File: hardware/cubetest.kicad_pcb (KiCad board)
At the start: 2 copper layers, 50.8 x 50.8 mm, 22 parts, among them J1 In, J10 GS2, J11 GS2, J2 Out, J3 pwr1, J4 pwr2, J5 USB_OTG, J6 GS3, J7 GS3, J8 GS3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

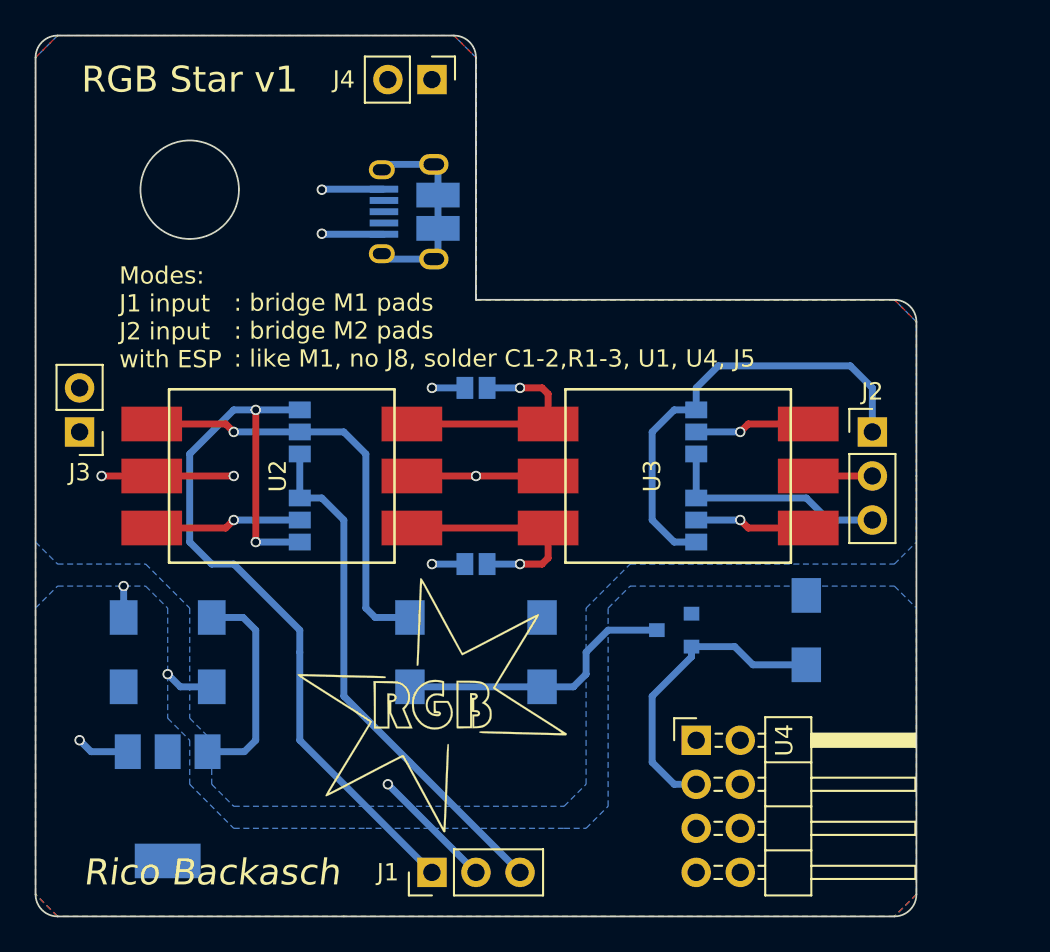
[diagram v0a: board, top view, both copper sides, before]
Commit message: remove solder bridges
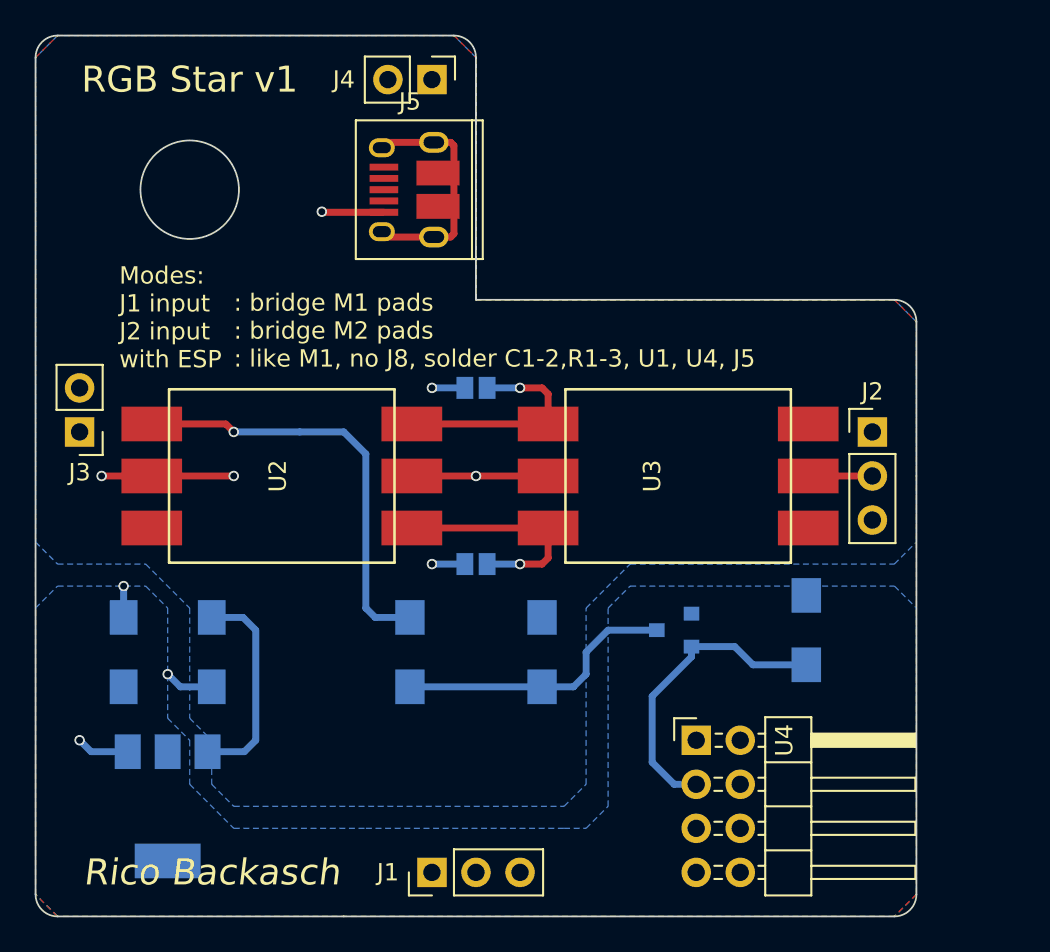
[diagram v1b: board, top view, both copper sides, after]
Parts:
- removed G***: LOGO, cubetest:LOGO
- removed J6, J7, J8, J9: GS3, Connect:GS3
- J5: moved to F.Cu
- moved J5 1.27 mm to (146.1, 57.1), turned to 90 degrees
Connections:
- J1 pad 1: Net-(J1-Pad1) -> D1in
- J1 pad 3: Net-(J1-Pad3) -> D2in
- J2 pad 1: Net-(J2-Pad1) -> D1out
- J2 pad 3: Net-(J2-Pad3) -> D2out
- J5 pad 2: Net-(J5-Pad2) -> (no net)
- J5 pad 3: Net-(J5-Pad3) -> (no net)
- J5 pad 4: Net-(J5-Pad4) -> (no net)
- U4 pad 2: Net-(U4-Pad2) -> (no net)
- U4 pad 5: Net-(U4-Pad5) -> (no net)
- U4 pad 7: Net-(U4-Pad7) -> (no net)
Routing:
- net Net-(J1-Pad1): track 48.2 -> 0.00 mm, vias 2 -> 0
- net Net-(J1-Pad3): track 30.8 -> 0.00 mm
- net Net-(J2-Pad1): track 26.2 -> 0.00 mm
- net Net-(J2-Pad3): track 13.2 -> 0.00 mm
- net D2in: track 8.73 -> 0.63 mm, vias 1 -> 0
- net +5V: track 42.2 -> 35.0 mm, vias 5 -> 4
- net D1out: track 6.65 -> 0.00 mm, vias 1 -> 0
- net D2out: track 6.65 -> 0.00 mm, vias 1 -> 0
- net GND: track 15.1 -> 11.5 mm, vias 6 -> 5
- net Net-(J5-Pad6): track 12.3 -> 13.8 mm

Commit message: fix pcb, added new pwr
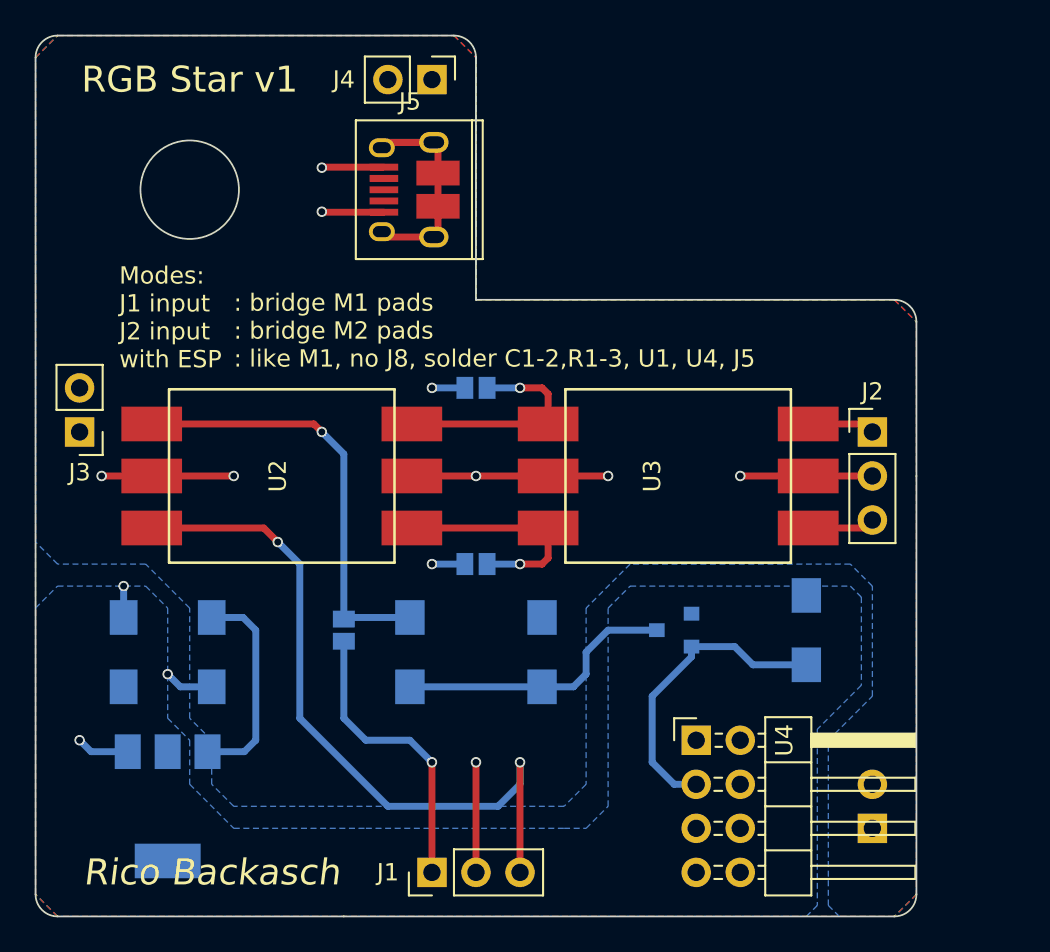
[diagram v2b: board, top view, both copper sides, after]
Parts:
- added J6: GS2, Connectors:GS2, B.Cu at (142.2, 82.5)
- added J7: pwr3, Pin_Headers:Pin_Header_Straight_1x02_Pitch2.54mm, B.Cu at (172.7, 94.0)
- J10, J11: footprint Connect:GS2 -> Connectors:GS2
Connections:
- J1 pad 1: D1in -> Net-(J1-Pad1)
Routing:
- net D2in: track 0.63 -> 41.9 mm, vias 0 -> 2
- net Net-(J1-Pad1): track 0.00 -> 16.9 mm, vias 0 -> 1
- net +5V: track 35.0 -> 48.7 mm, vias 4 -> 7
- net D1out: track 0.00 -> 3.89 mm
- net D2out: track 0.00 -> 3.89 mm
- net GND: track 11.5 -> 15.1 mm, vias 5 -> 6
- net Net-(J5-Pad6): track 13.8 -> 12.3 mm
